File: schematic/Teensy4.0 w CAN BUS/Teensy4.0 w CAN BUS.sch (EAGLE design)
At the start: 12 parts, among them U1 MAX13054ASA

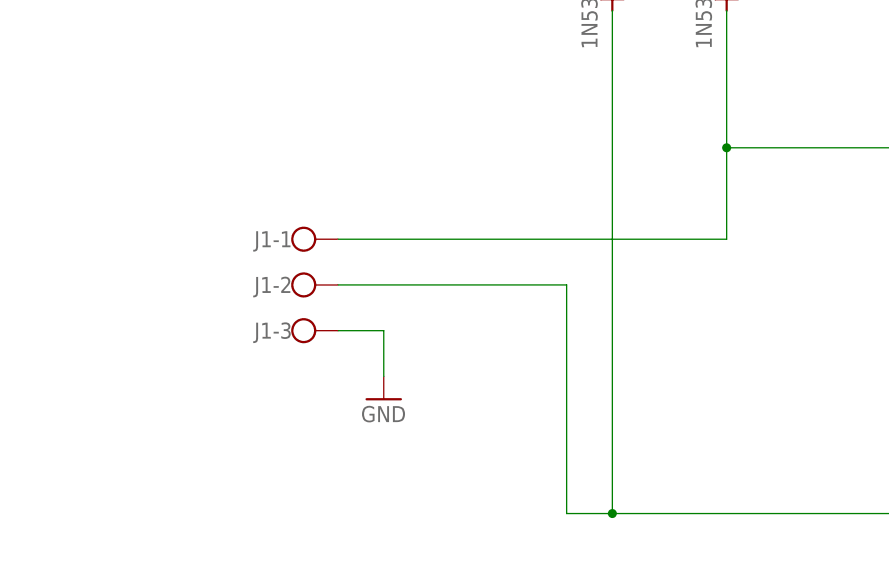
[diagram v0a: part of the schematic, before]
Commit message: Added military connectors to CAN Bus and added copper threading to PCB designs
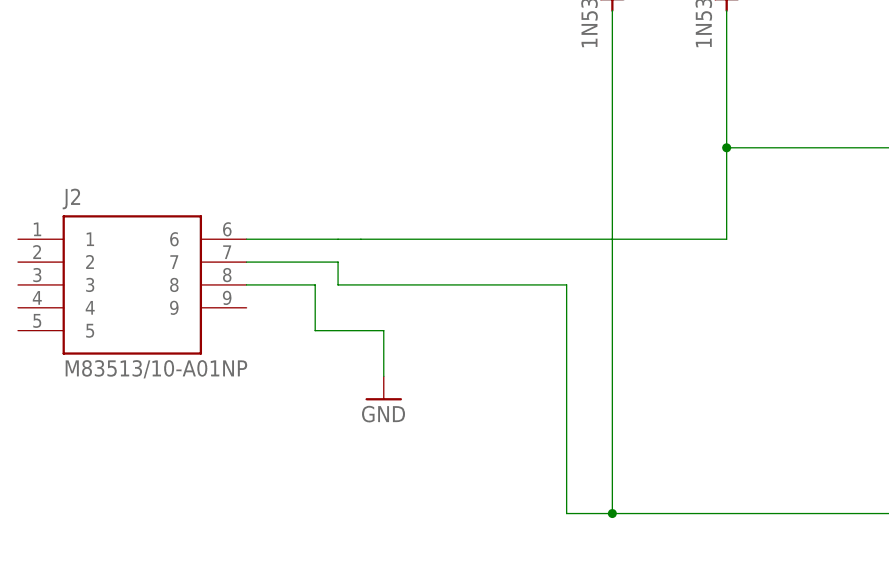
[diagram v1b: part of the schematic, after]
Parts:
- removed J1: (no value), con-wago-500:W237-103
- added J2: M83513/10-A01NP, M83513_10-A01NP:M83513/10-A01NP
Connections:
- net CAN_BUS: now also J2.6; no longer J1-1.KL
- net GND: now also J2.8; no longer J1-3.KL
- net N$5: now also J2.7; no longer J1-2.KL
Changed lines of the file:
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@@
 <part name="D3" library="diode" library_urn="urn:adsk.eagle:library:210" deviceset="1N5333" device="" package3d_urn="urn:adsk.eagle:package:43351/1"/>
 <part name="D4" library="diode" library_urn="urn:adsk.eagle:library:210" deviceset="1N5333" device="" package3d_urn="urn:adsk.eagle:package:43351/1"/>
-<part name="J1" library="con-wago-500" library_urn="urn:adsk.eagle:library:195" deviceset="W237-103" device="" package3d_urn="urn:adsk.eagle:package:10691/1"/>
 <part name="GND4" library="supply1" library_urn="urn:adsk.eagle:library:371" deviceset="GND" device=""/>
 <part name="GND5" library="supply1" library_urn="urn:adsk.eagle:library:371" deviceset="GND" device=""/>
+<part name="J2" library="M83513_10-A01NP" deviceset="M83513/10-A01NP" device=""/>
 </parts>
 <sheets>
@@
 <attribute name="VALUE" x="46.609" y="135.382" size="1.778" layer="96" rot="R90"/>
 </instance>
-<instance part="J1" gate="-1" x="-5.08" y="99.06" smashed="yes">
-<attribute name="NAME" x="-5.08" y="99.949" size="1.778" layer="95" rot="R180"/>
-</instance>
-<instance part="J1" gate="-2" x="-5.08" y="93.98" smashed="yes">
-<attribute name="NAME" x="-5.08" y="94.869" size="1.778" layer="95" rot="R180"/>
-</instance>
-<instance part="J1" gate="-3" x="-5.08" y="88.9" smashed="yes">
-<attribute name="VALUE" x="-7.62" y="85.217" size="1.778" layer="96"/>
-<attribute name="NAME" x="-5.08" y="89.789" size="1.778" layer="95" rot="R180"/>
-</instance>
 <instance part="GND4" gate="1" x="38.1" y="147.32" smashed="yes" rot="R180">
 <attribute name="VALUE" x="40.64" y="149.86" size="1.778" layer="96" rot="R180"/>
@@
 <instance part="GND5" gate="1" x="5.08" y="81.28" smashed="yes">
 <attribute name="VALUE" x="2.54" y="78.74" size="1.778" layer="96"/>
+</instance>
+<instance part="J2" gate="G$1" x="-22.86" y="93.98" smashed="yes">
+<attribute name="NAME" x="-30.48" y="102.87" size="1.778" layer="95"/>
+<attribute name="VALUE" x="-30.48" y="83.82" size="1.778" layer="96"/>
 </instance>
 </instances>
@@
 </segment>
 <segment>
-<pinref part="J1" gate="-3" pin="KL"/>
-<wire x1="0" y1="88.9" x2="5.08" y2="88.9" width="0.1524" layer="91"/>
+<wire x1="-2.54" y1="88.9" x2="5.08" y2="88.9" width="0.1524" layer="91"/>
 <pinref part="GND5" gate="1" pin="GND"/>
 <wire x1="5.08" y1="88.9" x2="5.08" y2="83.82" width="0.1524" layer="91"/>
+<pinref part="J2" gate="G$1" pin="8"/>
+<wire x1="-10.16" y1="93.98" x2="-2.54" y2="93.98" width="0.1524" layer="91"/>
+<wire x1="-2.54" y1="93.98" x2="-2.54" y2="88.9" width="0.1524" layer="91"/>
 </segment>
 <segment>
@@
 <wire x1="30.48" y1="124.46" x2="30.48" y2="68.58" width="0.1524" layer="91"/>
 <wire x1="30.48" y1="68.58" x2="66.04" y2="68.58" width="0.1524" layer="91"/>
-<pinref part="J1" gate="-2" pin="KL"/>
 <wire x1="0" y1="93.98" x2="25.4" y2="93.98" width="0.1524" layer="91"/>
 <wire x1="25.4" y1="93.98" x2="25.4" y2="68.58" width="0.1524" layer="91"/>
 <wire x1="25.4" y1="68.58" x2="30.48" y2="68.58" width="0.1524" layer="91"/>
 <junction x="30.48" y="68.58"/>
+<pinref part="J2" gate="G$1" pin="7"/>
+<wire x1="-10.16" y1="96.52" x2="0" y2="96.52" width="0.1524" layer="91"/>
+<wire x1="0" y1="96.52" x2="0" y2="93.98" width="0.1524" layer="91"/>
 </segment>
 </net>
@@
 <wire x1="43.18" y1="124.46" x2="43.18" y2="109.22" width="0.1524" layer="91"/>
 <wire x1="43.18" y1="109.22" x2="66.04" y2="109.22" width="0.1524" layer="91"/>
-<pinref part="J1" gate="-1" pin="KL"/>
-<wire x1="0" y1="99.06" x2="43.18" y2="99.06" width="0.1524" layer="91"/>
+<wire x1="0" y1="99.06" x2="2.54" y2="99.06" width="0.1524" layer="91"/>
+<wire x1="2.54" y1="99.06" x2="43.18" y2="99.06" width="0.1524" layer="91"/>
 <wire x1="43.18" y1="99.06" x2="43.18" y2="109.22" width="0.1524" layer="91"/>
 <junction x="43.18" y="109.22"/>
+<pinref part="J2" gate="G$1" pin="6"/>
+<wire x1="-10.16" y1="99.06" x2="0" y2="99.06" width="0.1524" layer="91"/>
 </segment>
 </net>
